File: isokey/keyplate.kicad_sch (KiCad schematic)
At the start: 170 parts, among them SW1 Cherry, SW2 Cherry, SW3 Cherry, SW4 Cherry, SW5 Cherry

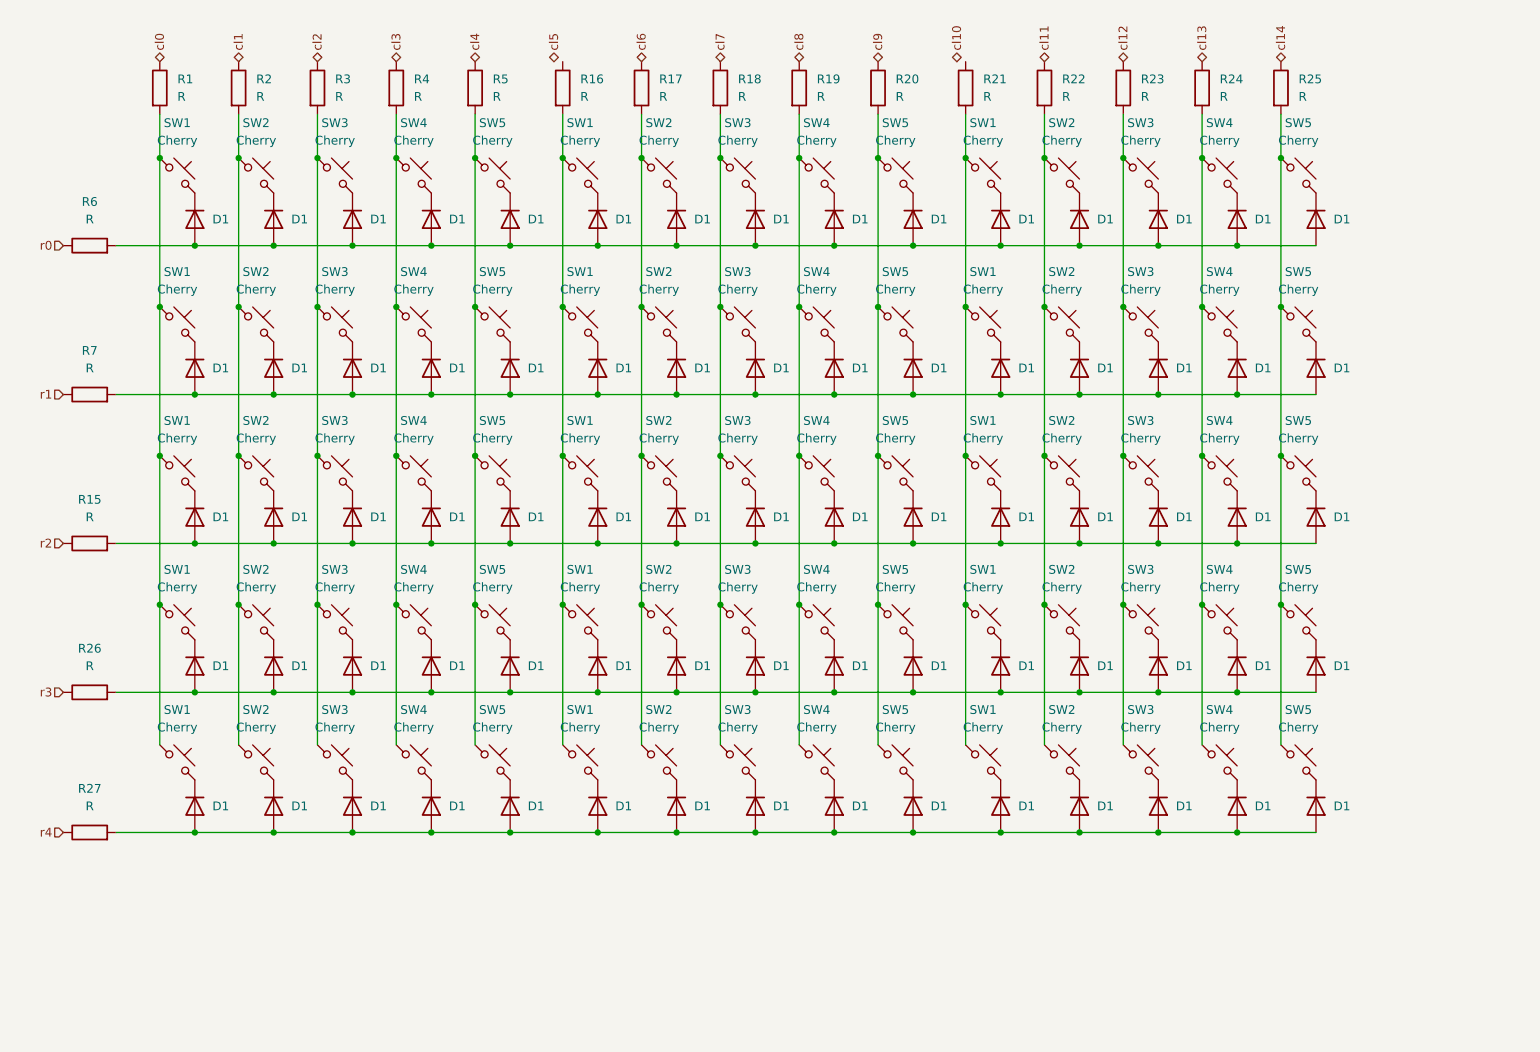
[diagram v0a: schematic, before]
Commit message: Add leds and extra connectors
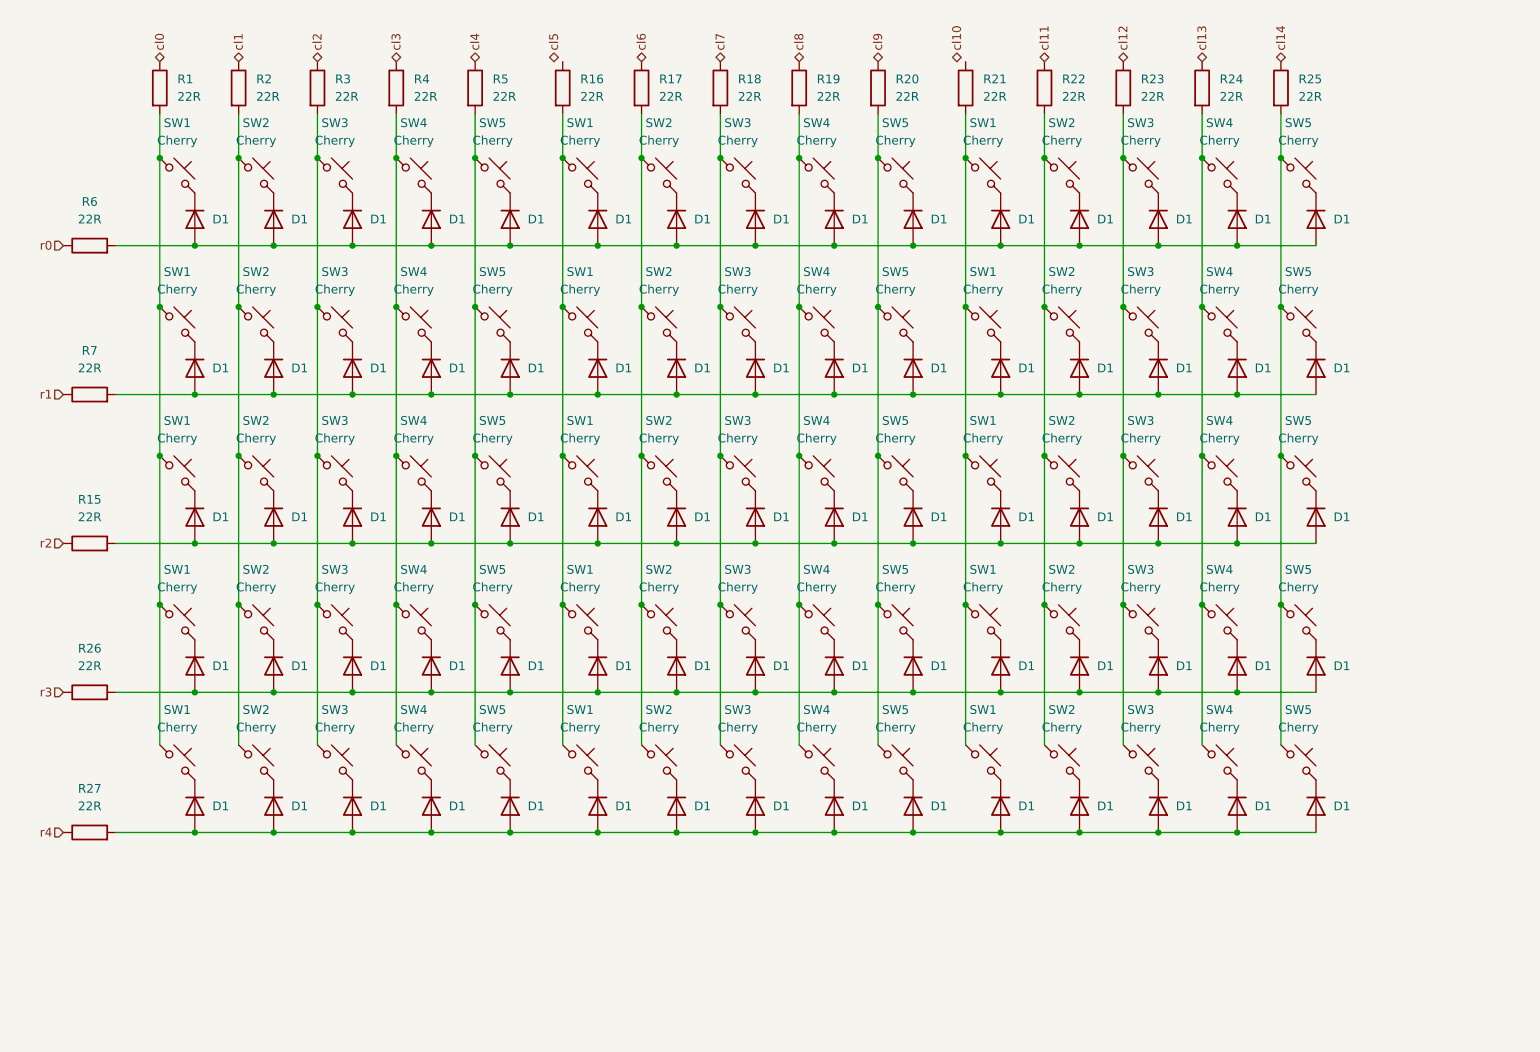
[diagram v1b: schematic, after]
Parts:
- R1, R15, R16, R17, R18, R19, R2, R20, R21, R22, R23, R24, R25, R26, R27, R3, R4, R5, R6, R7: value R -> 22R
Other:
- company: (none) -> IsoKey - asterix24@gmail.com
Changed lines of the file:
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@@
 (kicad_sch (version 20230121) (generator eeschema)
   (paper "A4")
+  (title_block
+    (date "2023-08-15")
+    (rev "0")
+    (company "IsoKey - asterix24@gmail.com")
+  )
   (junction (at 111.76 139.7) (diameter 0) (color 0 0 0 0)
   )
@@
       (effects (font (size 1.27 1.27)) (justify left))
     )
-    (property "Value" "R" (at 62.23 33.02 0)
+    (property "Value" "22R" (at 62.23 33.02 0)
       (effects (font (size 1.27 1.27)) (justify left))
     )
@@
       (effects (font (size 1.27 1.27)) (justify left))
     )
-    (property "Value" "R" (at 179.07 33.02 0)
+    (property "Value" "22R" (at 179.07 33.02 0)
       (effects (font (size 1.27 1.27)) (justify left))
     )
@@
       (effects (font (size 1.27 1.27)) (justify left))
     )
-    (property "Value" "R" (at 109.22 33.02 0)
+    (property "Value" "22R" (at 109.22 33.02 0)
       (effects (font (size 1.27 1.27)) (justify left))
     )
@@
       (effects (font (size 1.27 1.27)) (justify left))
     )
-    (property "Value" "R" (at 120.65 33.02 0)
+    (property "Value" "22R" (at 120.65 33.02 0)
       (effects (font (size 1.27 1.27)) (justify left))
     )
@@
       (effects (font (size 1.27 1.27)))
     )
-    (property "Value" "R" (at 38.1 72.39 90)
+    (property "Value" "22R" (at 38.1 72.39 90)
       (effects (font (size 1.27 1.27)))
     )
@@
       (effects (font (size 1.27 1.27)) (justify left))
     )
-    (property "Value" "R" (at 50.8 33.02 0)
+    (property "Value" "22R" (at 50.8 33.02 0)
       (effects (font (size 1.27 1.27)) (justify left))
     )
@@
       (effects (font (size 1.27 1.27)) (justify left))
     )
-    (property "Value" "R" (at 143.51 33.02 0)
+    (property "Value" "22R" (at 143.51 33.02 0)
       (effects (font (size 1.27 1.27)) (justify left))
     )
@@
       (effects (font (size 1.27 1.27)) (justify left))
     )
-    (property "Value" "R" (at 73.66 33.02 0)
+    (property "Value" "22R" (at 73.66 33.02 0)
       (effects (font (size 1.27 1.27)) (justify left))
     )
@@
       (effects (font (size 1.27 1.27)) (justify left))
     )
-    (property "Value" "R" (at 154.94 33.02 0)
+    (property "Value" "22R" (at 154.94 33.02 0)
       (effects (font (size 1.27 1.27)) (justify left))
     )
@@
       (effects (font (size 1.27 1.27)))
     )
-    (property "Value" "R" (at 38.1 50.8 90)
+    (property "Value" "22R" (at 38.1 50.8 90)
       (effects (font (size 1.27 1.27)))
     )
@@
       (effects (font (size 1.27 1.27)))
     )
-    (property "Value" "R" (at 38.1 115.57 90)
+    (property "Value" "22R" (at 38.1 115.57 90)
       (effects (font (size 1.27 1.27)))
     )
@@
       (effects (font (size 1.27 1.27)))
     )
-    (property "Value" "R" (at 38.1 93.98 90)
+    (property "Value" "22R" (at 38.1 93.98 90)
       (effects (font (size 1.27 1.27)))
     )
@@
       (effects (font (size 1.27 1.27)) (justify left))
     )
-    (property "Value" "R" (at 190.5 33.02 0)
+    (property "Value" "22R" (at 190.5 33.02 0)
       (effects (font (size 1.27 1.27)) (justify left))
     )
@@
       (effects (font (size 1.27 1.27)) (justify left))
     )
-    (property "Value" "R" (at 96.52 33.02 0)
+    (property "Value" "22R" (at 96.52 33.02 0)
       (effects (font (size 1.27 1.27)) (justify left))
     )
@@
       (effects (font (size 1.27 1.27)) (justify left))
     )
-    (property "Value" "R" (at 167.64 33.02 0)
+    (property "Value" "22R" (at 167.64 33.02 0)
       (effects (font (size 1.27 1.27)) (justify left))
     )
@@
       (effects (font (size 1.27 1.27)) (justify left))
     )
-    (property "Value" "R" (at 201.93 33.02 0)
+    (property "Value" "22R" (at 201.93 33.02 0)
       (effects (font (size 1.27 1.27)) (justify left))
     )
@@
       (effects (font (size 1.27 1.27)) (justify left))
     )
-    (property "Value" "R" (at 85.09 33.02 0)
+    (property "Value" "22R" (at 85.09 33.02 0)
       (effects (font (size 1.27 1.27)) (justify left))
     )
@@
       (effects (font (size 1.27 1.27)))
     )
-    (property "Value" "R" (at 38.1 135.89 90)
+    (property "Value" "22R" (at 38.1 135.89 90)
       (effects (font (size 1.27 1.27)))
     )
@@
       (effects (font (size 1.27 1.27)) (justify left))
     )
-    (property "Value" "R" (at 213.36 33.02 0)
+    (property "Value" "22R" (at 213.36 33.02 0)
       (effects (font (size 1.27 1.27)) (justify left))
     )
@@
       (effects (font (size 1.27 1.27)) (justify left))
     )
-    (property "Value" "R" (at 132.08 33.02 0)
+    (property "Value" "22R" (at 132.08 33.02 0)
       (effects (font (size 1.27 1.27)) (justify left))
     )

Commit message: Place all sw
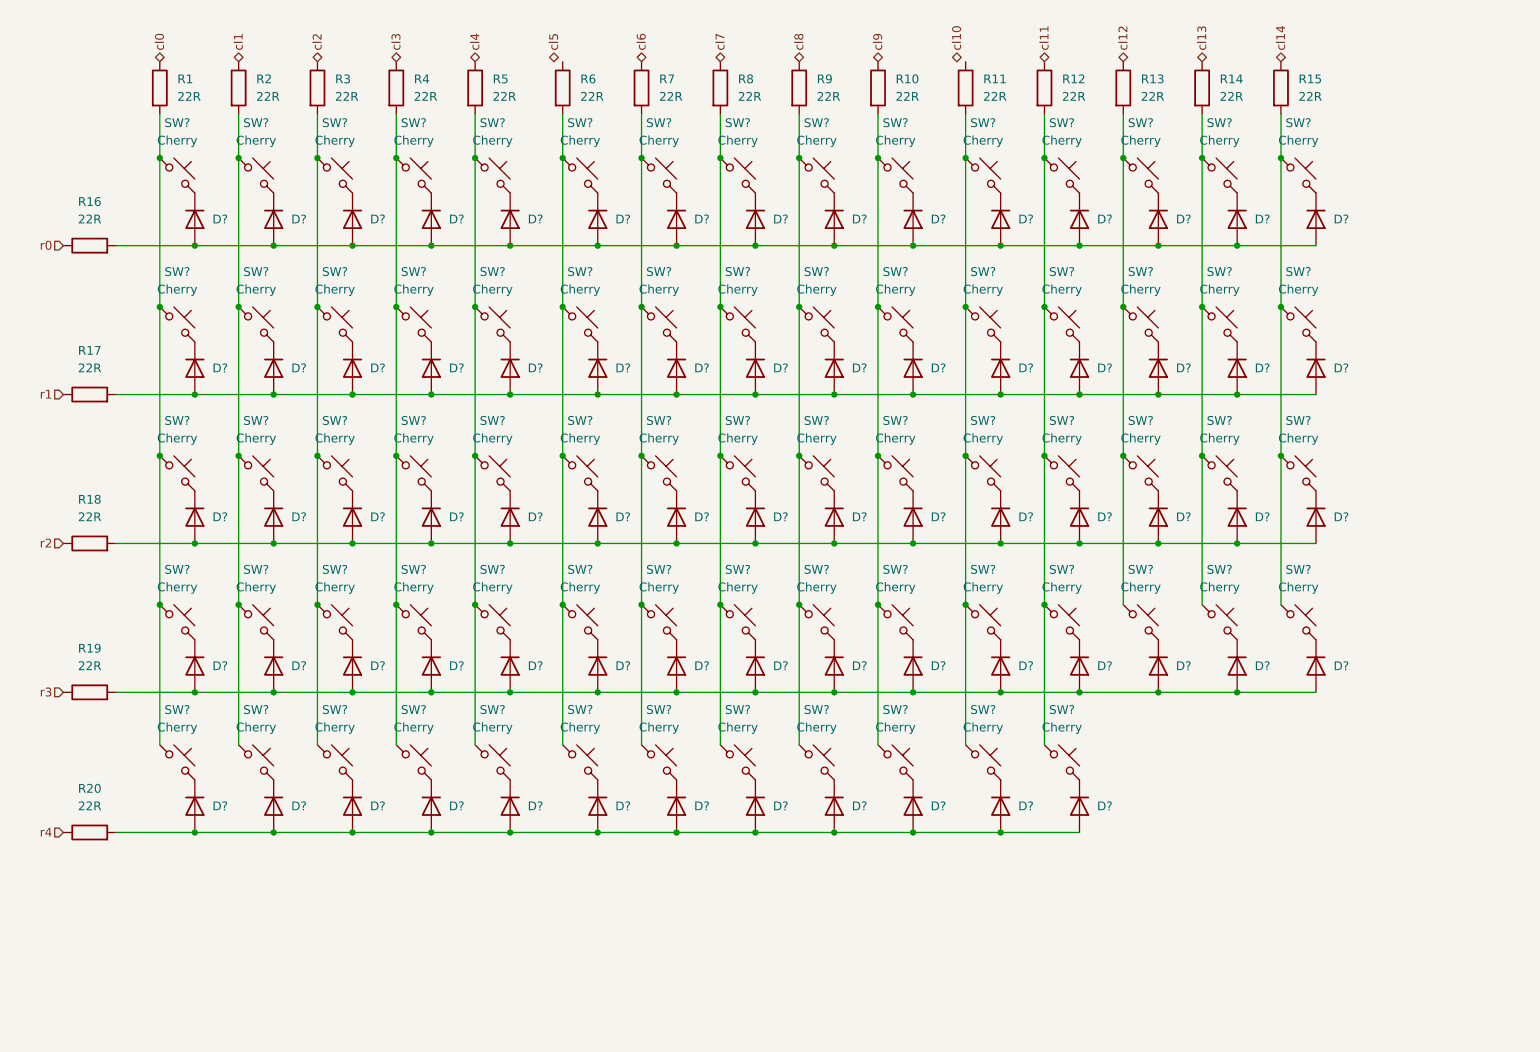
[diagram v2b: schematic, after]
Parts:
- removed D1 (x3): 1N4448W, Diode_SMD:D_SOD-123, symbol Diode:1N4448W
- removed R6: 22R, symbol Device:R
- removed SW3, SW4, SW5: Cherry, symbol Switch:SW_Push_45deg
- added R16: 22R, symbol Device:R
- SW? (x15): renamed from SW2; footprint (none) -> Button_Switch_Keyboard:SW_MX
- SW? (x15): renamed from SW1; footprint (none) -> Button_Switch_Keyboard:SW_MX
- SW? (x14): renamed from SW4; footprint (none) -> Button_Switch_Keyboard:SW_MX
- SW? (x14): renamed from SW5; footprint (none) -> Button_Switch_Keyboard:SW_MX
- SW? (x14): renamed from SW3; footprint (none) -> Button_Switch_Keyboard:SW_MX
- renumbered D1 to D?, R20 to R10, R21 to R11, R22 to R12, R23 to R13, R24 to R14, R25 to R15, R7 to R17, R15 to R18, R26 to R19, R27 to R20, R16 to R6, R17 to R7, R18 to R8, R19 to R9
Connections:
- net r0: now also R16.1
- net at D?.2 (A), D?.2 (A), D?.2 (A)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: now also R16.2

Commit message: Place switch and leds
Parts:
- R1, R10, R11, R12, R13, R14, R15, R16, R17, R18, R19, R2, R20, R3, R4, R5, R6, R7, R8, R9: footprint (none) -> Resistor_SMD:R_0603_1608Metric_Pad0.98x0.95mm_HandSolder
- SW? (x72): footprint Button_Switch_Keyboard:SW_MX -> Button_Switch_Keyboard:Kailh_socket_MX_LED
